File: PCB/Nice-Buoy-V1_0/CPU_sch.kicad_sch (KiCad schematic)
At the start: 53 parts, among them J101 1051330011, J102 LEDSTRIP, J102 SW1, J102 SW2, J901 Display, Q8 2N7002, Q9 2N7002, SW3 ~{BOOT}, SW4 ~{RESET}, U101 SRV05-4, U102 CP2104-F03-GMR, U103 ESP32-WROOM-32E_(visible_peri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

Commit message: Buzzer added key readoud improved
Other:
- note added: "GPIO13 buzzer added"
- note added: "Not programming. DR0 should be connected toe GPIO0 now to GPIO2 Rework: connect GPIO0 to GPIO2 Pin 25 to 24 ESC signal to weak. Change R401 and R402 to 0 ohm"
- note removed: "Not programming. DR0 should be connected toe GPIO0 now to GPIO2 Rework: connect GPIO0 to GPIO2 Pin 25 to 24"
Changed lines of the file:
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@@
+    (effects (font (size 1.27 1.27)) (justify left bottom))
+  )
+  (text "GPIO13 buzzer added" (at 19.05 36.83 0)
     (effects (font (size 1.27 1.27)) (justify left bottom))
   )
@@
     (effects (font (size 1.27 1.27)) (justify left bottom))
   )
-  (text "Not programming.\nDR0 should be connected toe GPIO0 now to GPIO2\nRework: \nconnect GPIO0 to GPIO2\nPin 25 to 24"
+  (text "Not programming.\nDR0 should be connected toe GPIO0 now to GPIO2\nRework: \nconnect GPIO0 to GPIO2\nPin 25 to 24\nESC signal to weak. Change R401 and R402 to 0 ohm\n"
     (at 19.05 26.67 0)
     (effects (font (size 1.27 1.27)) (justify left bottom))

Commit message: dingus
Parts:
- renumbered C703 to C113, C703 to C114, D13 to D102, J901 to J102, J102 to J103, J102 to J104, J102 to J105, R106 to R108, R108 to R109, R108 to R110, R108 to R111, R108 to R112, R106 to R113, R106 to R114, R106 to R119, R106 to R120

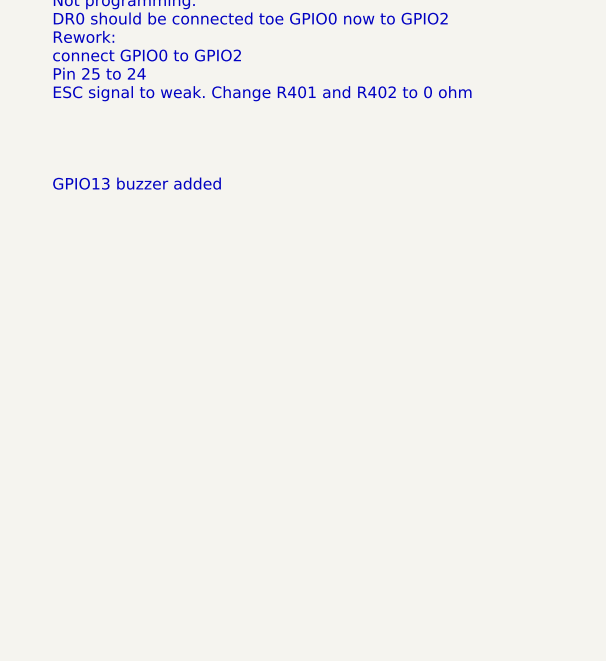
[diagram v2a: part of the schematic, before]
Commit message: New command structure
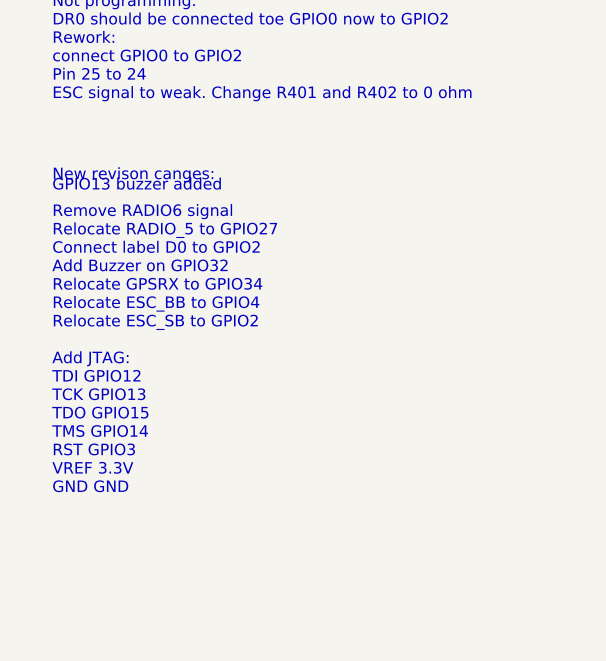
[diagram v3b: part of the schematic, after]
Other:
- note added: "New revison canges: Remove RADIO6 signal Relocate RADIO_5 to GPIO27 Connect label D0 to GPIO2 Add Buzzer on GPIO32 Relocate GPSRX to GPIO34 Relocate ESC_BB to GPIO4 Relocate ESC_SB to GPIO2 Add JTAG: TDI GPIO12 TCK GPIO13 TDO GPIO15 TMS GPIO14 RST GPIO3 VREF 3.3V GND GND"
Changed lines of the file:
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@@
+		)
+	)
+	(text "New revison canges:\n\nRemove RADIO6 signal\nRelocate RADIO_5 to GPIO27\nConnect label D0 to GPIO2\nAdd Buzzer on GPIO32\nRelocate GPSRX to GPIO34\nRelocate ESC_BB to GPIO4\nRelocate ESC_SB to GPIO2\n\nAdd JTAG:\nTDI GPIO12\nTCK GPIO13\nTDO GPIO15\nTMS GPIO14\nRST GPIO3\nVREF 3.3V\nGND GND\n\n"
+		(exclude_from_sim no)
+		(at 19.05 53.34 0)
+		(effects
+			(font
+				(size 1.27 1.27)
+			)
+			(justify left)
 		)
 	)
